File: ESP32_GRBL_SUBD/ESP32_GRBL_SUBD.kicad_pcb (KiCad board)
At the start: 2 copper layers, 91 x 67 mm, 76 parts, among them J1 DB25_Female_MountingHoles, J10 Screw_Terminal_01x02, J11 Screw_Terminal_01x02, J12 Screw_Terminal_01x02, J13 Screw_Terminal_01x02, J2 Micro_SD_Card, J3 Conn_01x19_Female, J3a1 Conn_01x19_Female, J4 Conn_01x19_Female, J4a1 Conn_01x19_Female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

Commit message: D-Sub Pin 14 could be either a input or an output because my CNC milling machine uses this pin to switch on the coolant. Untested PCB added
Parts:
- added R37: 0R, Resistor_SMD:R_0603_1608Metric, B.Cu at (134.6, 94.3)
- added R38: dnp, Resistor_SMD:R_0603_1608Metric, B.Cu at (134.6, 92.8)
- added R39: dnp, Resistor_SMD:R_0603_1608Metric, B.Cu at (134.6, 91.2)
- added R40: dnp, Resistor_SMD:R_0603_1608Metric, B.Cu at (151.1, 88.2)
- added R41: dnp, Resistor_SMD:R_0603_1608Metric, B.Cu at (151.1, 89.7)
- R21, R29: value 0R -> dnp
- R23, R30: value dnp -> 0R
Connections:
- J1 pad 10: /RESET -> /Z_LIM
- J1 pad 11: /X_LIM -> /RESET
- J1 pad 13: /Z_LIM -> /X_LIM
- J1 pad 14: /A_LIM -> /A_LIM-OUT9
- J3 pad 11: /Z_LIM_3V3 -> /X_LIM_3V3
- J3 pad 13: /X_LIM_3V3 -> /Z_LIM_3V3
- J3 pad 2: Net-(J3-Pad2) -> unconnected-(J3-Pad2)
- J3 pad 3: Net-(J3-Pad3) -> unconnected-(J3-Pad3)
- J3 pad 4: Net-(J3-Pad4) -> unconnected-(J3-Pad4)
- J3a1 pad 11: /Z_LIM_3V3 -> /X_LIM_3V3
- J3a1 pad 13: /X_LIM_3V3 -> /Z_LIM_3V3
- J3a1 pad 2: Net-(J3a1-Pad2) -> unconnected-(J3a1-Pad2)
- J3a1 pad 3: Net-(J3a1-Pad3) -> unconnected-(J3a1-Pad3)
- J3a1 pad 4: Net-(J3a1-Pad4) -> unconnected-(J3a1-Pad4)
- J4 pad 1: Net-(J4-Pad1) -> unconnected-(J4-Pad1)
- J4 pad 2: Net-(J4-Pad2) -> unconnected-(J4-Pad2)
- J4 pad 3: Net-(J4-Pad3) -> unconnected-(J4-Pad3)
- J4a1 pad 1: Net-(J4a1-Pad1) -> unconnected-(J4a1-Pad1)
- J4a1 pad 2: Net-(J4a1-Pad2) -> unconnected-(J4a1-Pad2)
- J4a1 pad 3: Net-(J4a1-Pad3) -> unconnected-(J4a1-Pad3)
- Q4 pad 2: /RESET_3V3 -> /Z_LIM_3V3
- Q4 pad 3: /RESET -> /Z_LIM
- Q5 pad 2: /X_LIM_3V3 -> /RESET_3V3
- Q5 pad 3: /X_LIM -> /RESET
- Q7 pad 2: /Z_LIM_3V3 -> /X_LIM_3V3
- Q7 pad 3: /Z_LIM -> /X_LIM
- R11 pad 2: /RESET_3V3 -> /Z_LIM_3V3
- R12 pad 2: /X_LIM_3V3 -> /RESET_3V3
- R14 pad 2: /Z_LIM_3V3 -> /X_LIM_3V3
- R17 pad 2: /RESET -> /Z_LIM
- R18 pad 2: /X_LIM -> /RESET
- R20 pad 2: /Z_LIM -> /X_LIM
- U2 pad 11: Net-(U2-Pad11) -> /OUT9
- U2 pad 12: Net-(U2-Pad12) -> unconnected-(U2-Pad12)
- U2 pad 13: Net-(U2-Pad13) -> unconnected-(U2-Pad13)
- U2 pad 14: Net-(U2-Pad14) -> unconnected-(U2-Pad14)
- U2 pad 15: Net-(U2-Pad15) -> unconnected-(U2-Pad15)
- U2 pad 9: GND -> /OUT3_3V3
- U3 pad 6: /Z_LIM_3V3 -> /X_LIM_3V3
- U3 pad 8: /X_LIM_3V3 -> /Z_LIM_3V3
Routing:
- net /Z_LIM_3V3: track 77.4 -> 64.5 mm
- net /X_LIM_3V3: track 64.5 -> 77.4 mm
- net /A_LIM-OUT9: track 0.00 -> 12.7 mm, vias 0 -> 1
- net /STEP_ENABLE: track 77.6 -> 87.4 mm, vias 7 -> 8
- net /A_LIM: track 16.2 -> 7.53 mm, vias 0 -> 1
- net /OUT3_3V3: track 0.00 -> 8.53 mm
- net /RESET_3V3: track 4.20 -> 10.9 mm
- net /Spindle_EN_3V3: track 71.1 -> 77.2 mm
- net /COOLANT_3V3: track 80.0 -> 82.8 mm
- net /Z_LIM: track 9.61 -> 12.3 mm
- net /OUT9: track 0.00 -> 2.24 mm
- net /X_LIM: track 11.0 -> 9.61 mm
- net /RESET: track 12.3 -> 11.0 mm
- net /Spindle_PWM_3V3: track 26.9 -> 26.2 mm
- net GND: vias 66 -> 67
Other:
- net class Default removed
- board text added: "TS 2022"
- board text added: "https://github.com/RunningPenguin/ESP32_GRBL_SUBD"
- board text removed: "JS 2020"

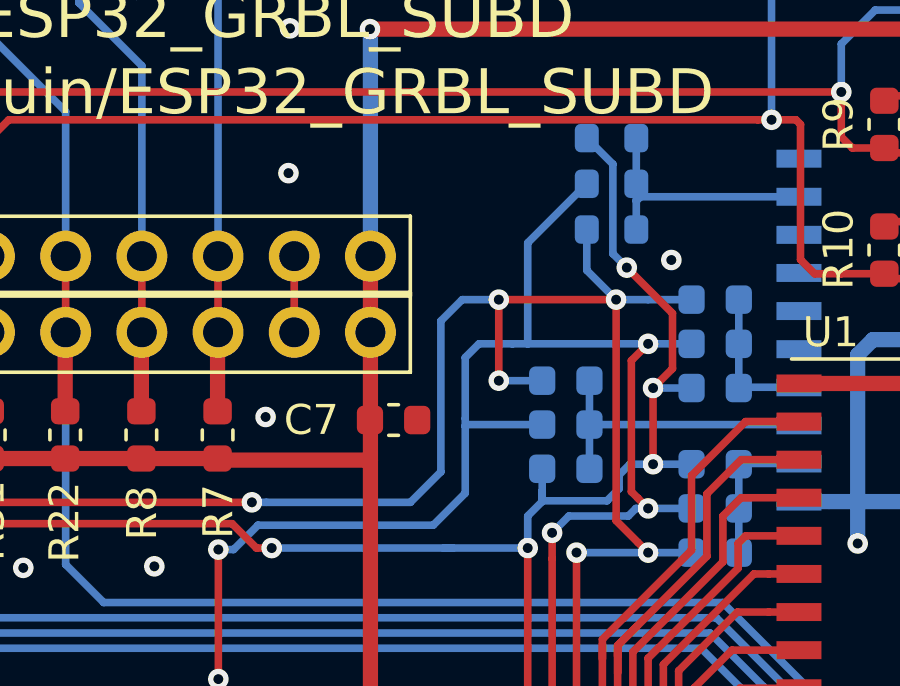
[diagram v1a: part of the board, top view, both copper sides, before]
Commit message: One unused output pin resistor to GND added. The logic level converter shouldnt be floating
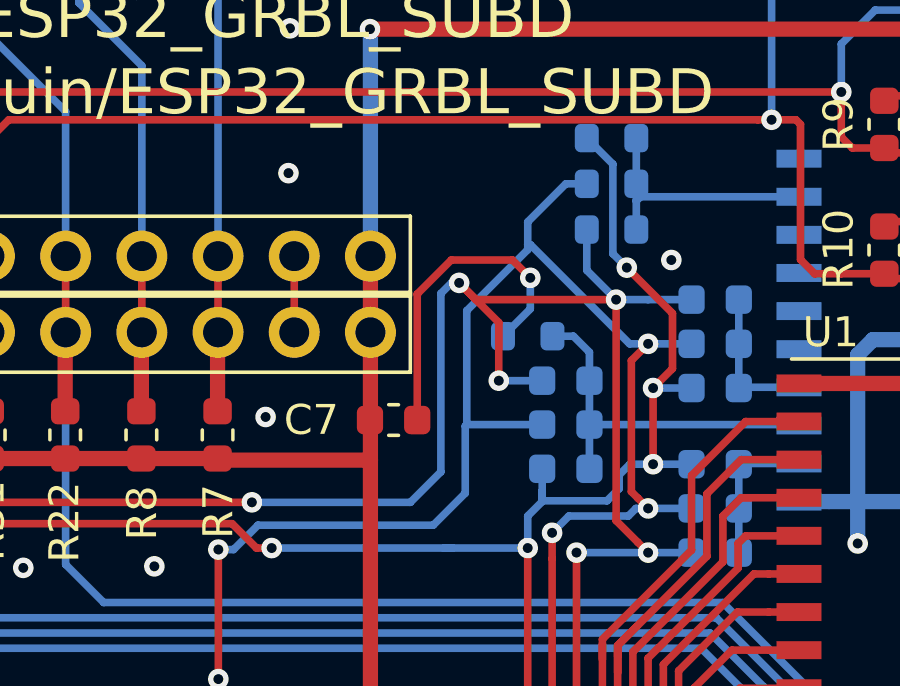
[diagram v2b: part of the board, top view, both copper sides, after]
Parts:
- added R42: 0R, Resistor_SMD:R_0603_1608Metric, B.Cu at (131.8, 97.8)
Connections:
- net /ENABLE renamed /BOOST
- net /OUT1 renamed /ENABLE_SPINDEL
- net /OUT2 renamed //SLEEP
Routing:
- net GND: track 13.9 -> 24.9 mm, vias 67 -> 68
- net /ENABLE_3V3: track 9.93 -> 12.3 mm
- net /COOLANT_3V3: track 82.8 -> 84.9 mm
- net /Spindle_EN_3V3: track 77.2 -> 78.0 mm

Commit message: mapped UART0 to screw header
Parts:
- added J14: Screw_Terminal_01x02, TerminalBlock_MetzConnect:TerminalBlock_MetzConnect_Type055_RT01502HDWU_1x02_P5.00mm_Horizontal, F.Cu at (87.1, 135.2)
- moved J12 4.97 mm to (97.8, 135.2)
- moved J11 3.64 mm to (108.4, 135.2)
- moved J13 2.31 mm to (119.1, 135.2)
- moved J10 1.03 mm to (129.8, 135.2)
- moved D3 0.56 mm to (142.1, 136.2)
- moved R34 0.56 mm to (142.1, 133.1)
- moved D2 0.56 mm to (143.8, 136.2)
- moved D4 0.56 mm to (140.4, 136.2)
- moved D5 0.56 mm to (138.6, 136.2)
- moved R33 0.56 mm to (143.8, 133.1)
- moved R35 0.56 mm to (140.4, 133.1)
- moved R36 0.56 mm to (138.6, 133.1)
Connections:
- J10 pad 1: /STEP_EN_5V -> /SPINDLE_PWM_5V
- J12 pad 1: /COOLANT_5V -> /STEP_EN_5V
- J13 pad 1: /SPINDLE_PWM_5V -> /COOLANT_5V
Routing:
- net /U0RX: track 2.54 -> 37.0 mm
- net /U0TX: track 2.54 -> 33.3 mm
- net /COOLANT_5V: track 46.0 -> 18.2 mm
- net /STEP_EN_5V: track 10.9 -> 37.5 mm, vias 1 -> 0
- net /SPINDLE_PWM_5V: track 23.4 -> 8.57 mm
- net /SPINDLE_EN_5V: track 34.1 -> 27.9 mm, vias 1 -> 0
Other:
- board text added: "RX-UART0-TX"
- board text added: "Step_EN"
- board text removed: "Step enable"

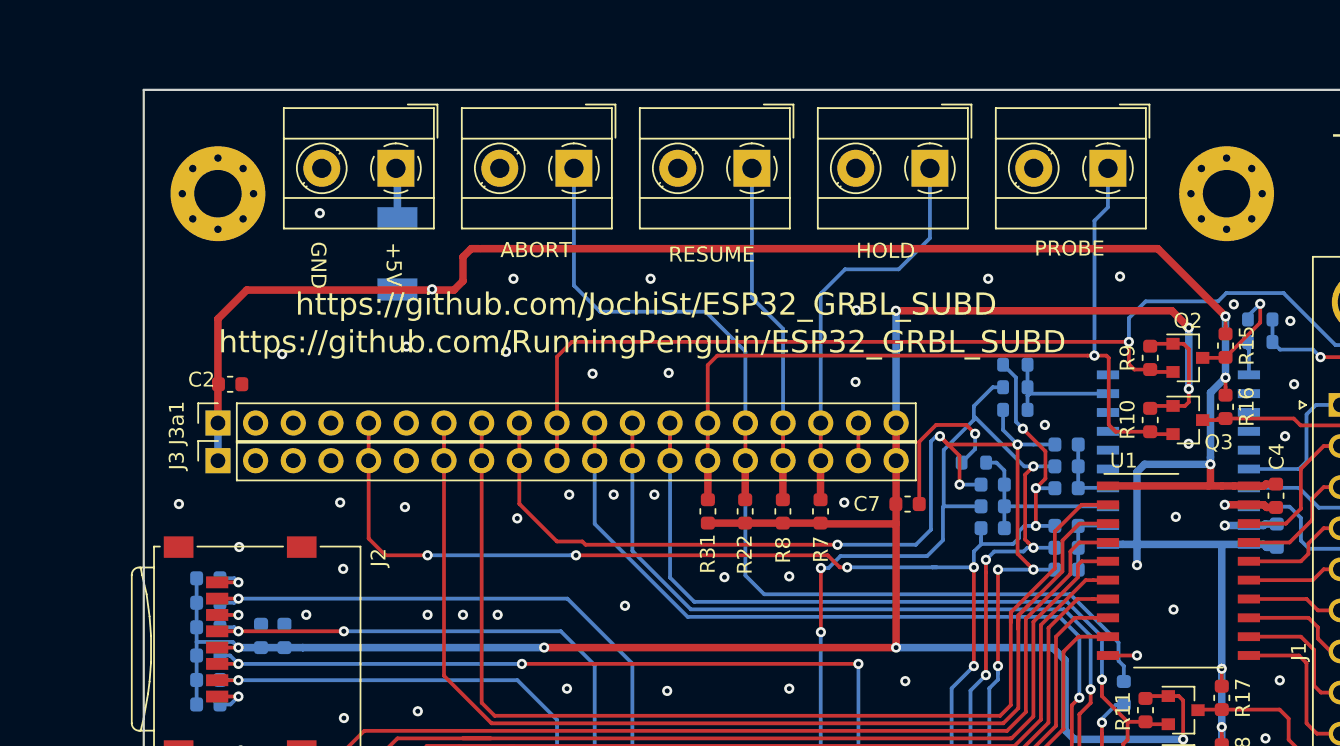
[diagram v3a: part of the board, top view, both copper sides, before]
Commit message: wired Axis a to screw terminals
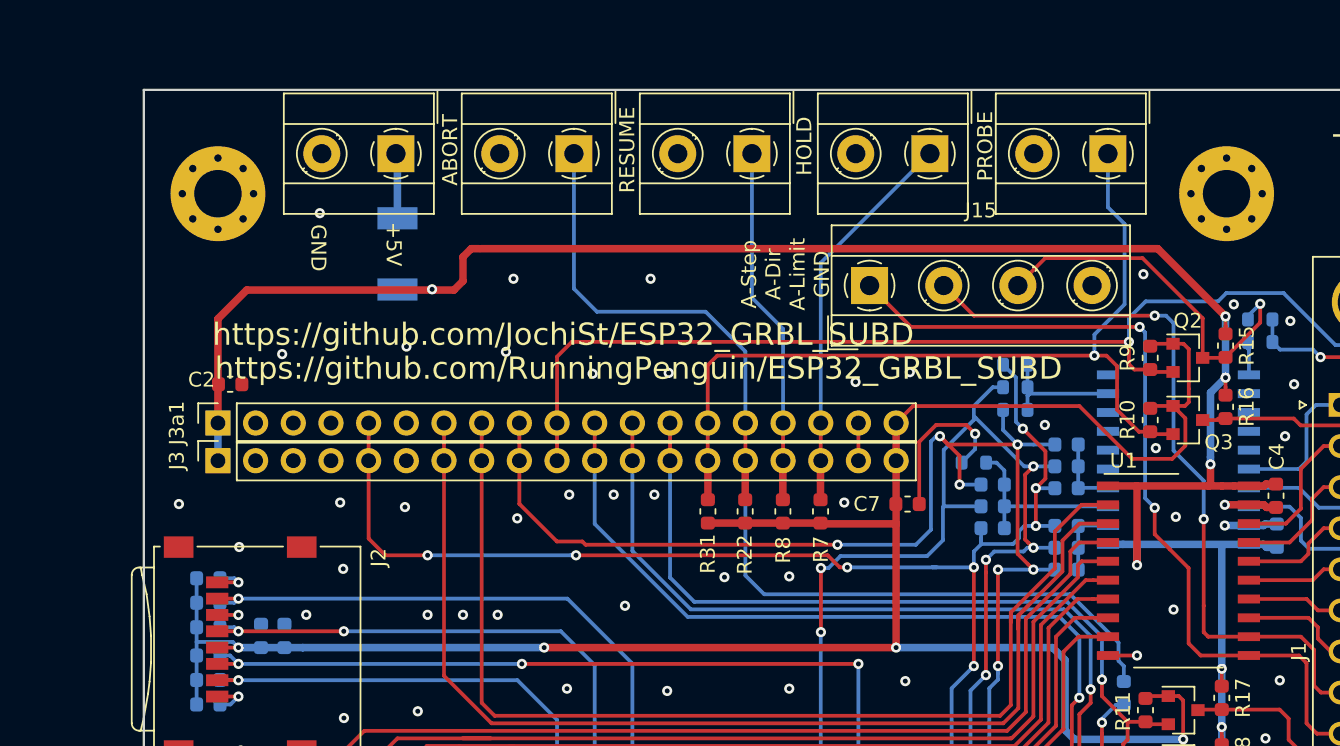
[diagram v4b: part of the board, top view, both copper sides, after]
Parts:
- added J15: Screw_Terminal_01x04, TerminalBlock_MetzConnect:TerminalBlock_MetzConnect_Type055_RT01504HDWU_1x04_P5.00mm_Horizontal, F.Cu at (124.7, 85.9)
- R32, R41: value dnp -> 0R
- moved J9 0.99 mm to (104.8, 77.0)
- moved J5 0.99 mm to (92.8, 77.0)
- moved J6 0.99 mm to (140.8, 77.0)
- moved J7 0.99 mm to (128.8, 77.0)
- moved J8 0.99 mm to (116.8, 77.0)
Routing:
- net /A_STEP: track 10.7 -> 57.2 mm, vias 0 -> 2
- net /A_DIR: track 9.15 -> 50.5 mm, vias 0 -> 2
- net /A_LIM: track 7.53 -> 25.1 mm
- net +3V3: track 180.0 -> 172.9 mm, vias 8 -> 5
- net +5V: track 192.1 -> 187.4 mm
- net /HOLD: track 27.8 -> 26.4 mm
- net +VDC: track 3.37 -> 4.40 mm
- net /PROBE_3V3: track 58.9 -> 59.6 mm
- net /RESUME: track 23.5 -> 24.2 mm
- net /ABORT: track 69.4 -> 70.0 mm
- net GND: vias 68 -> 67
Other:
- board text added: "A-Step A-Dir A-Limit GND"
